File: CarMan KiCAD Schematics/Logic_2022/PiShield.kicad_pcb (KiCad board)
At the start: 2 copper layers, 57.8 x 76.4 mm, 20 parts, among them J1 J2 NI I2C, J2 J4 GLV BOB, J3 PICAN 2 Connector, J4 Motor Controller Header, J5 TSI Header, J6 PICAN 2 Connector, U1 RaspberryPi3, U10 BNO_055, U11 Raspberry_Pi_RTC

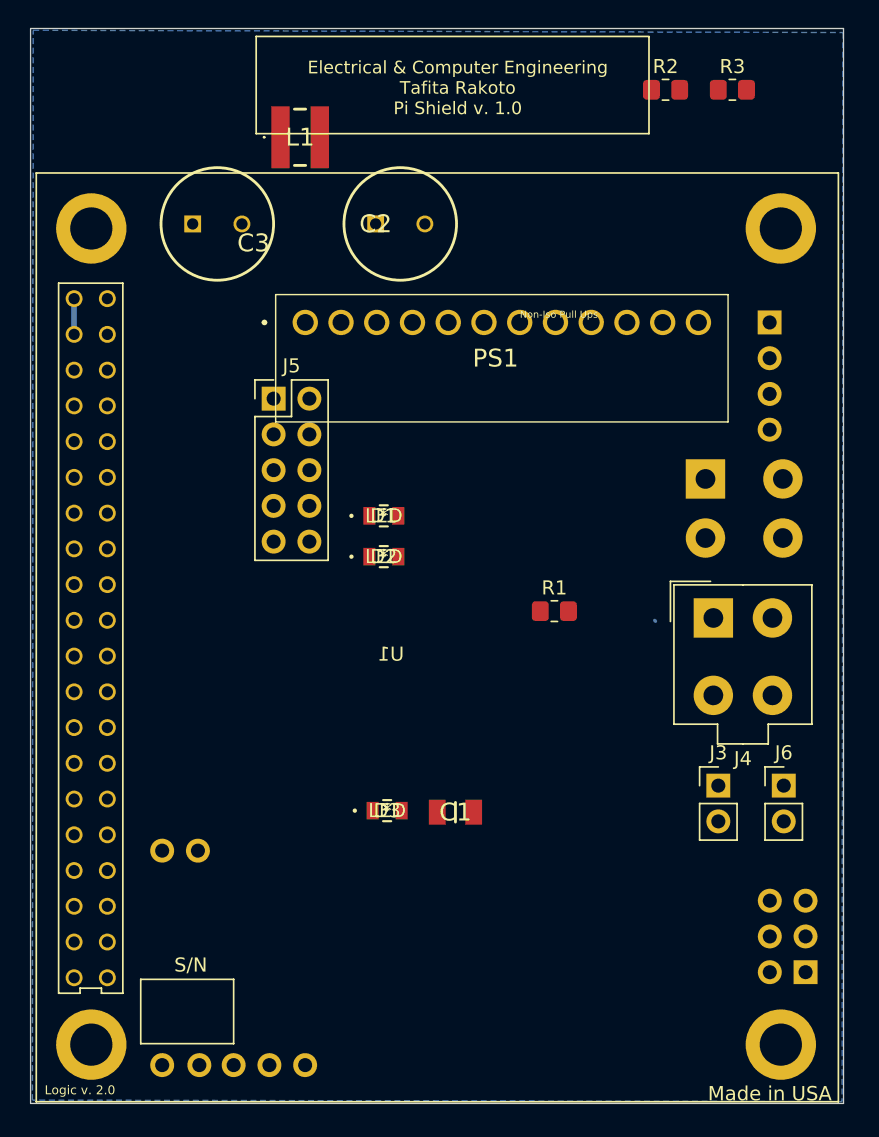
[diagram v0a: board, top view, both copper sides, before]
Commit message: Update the PCB layout with the wiring connected
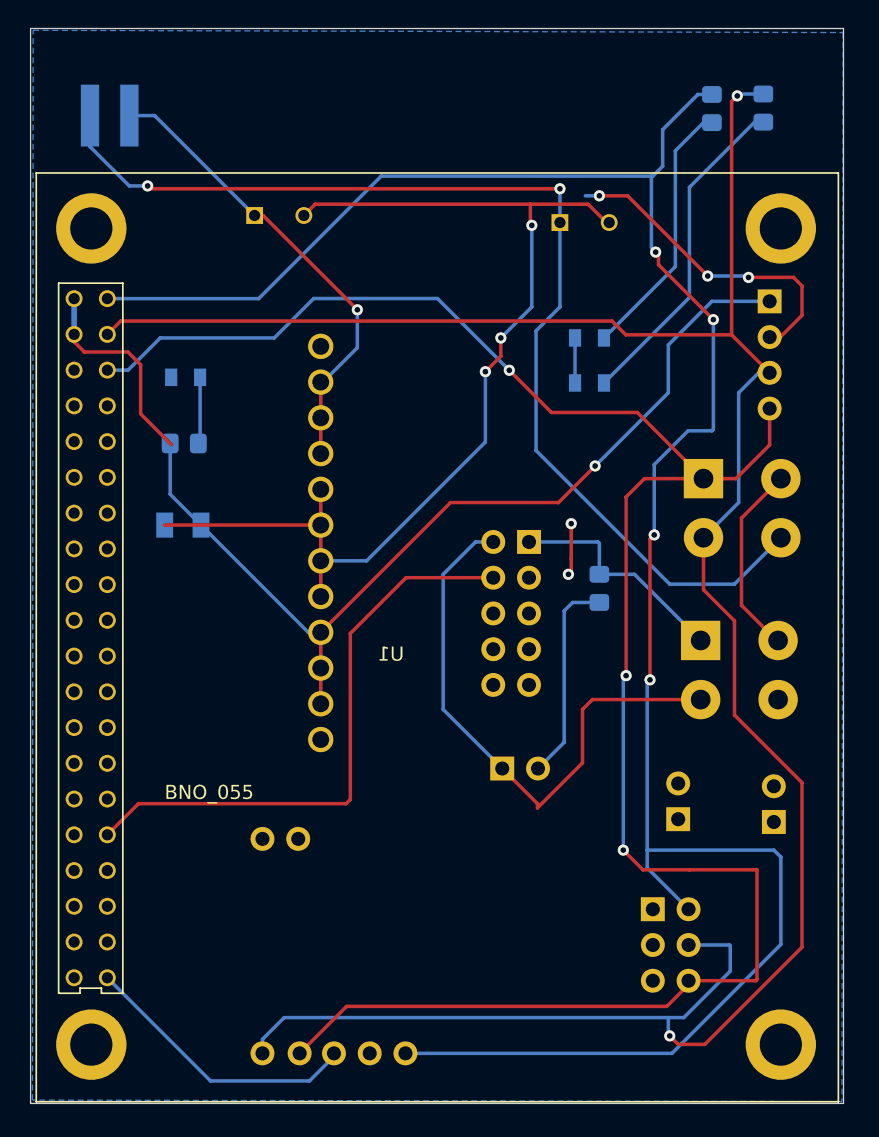
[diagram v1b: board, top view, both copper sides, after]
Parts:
- added J7: CAN Testing Header, Connector_PinHeader_2.54mm:PinHeader_1x02_P2.54mm_Vertical, B.Cu at (204.0, 91.7)
- added R4: 120, Resistor_SMD:R_0805_2012Metric_Pad1.20x1.40mm_HandSolder, B.Cu at (210.9, 78.9)
- C1, C2, C3, D1, D2, D3, J3, J4, J5, J6, L1, PS1, R1, R2, R3: moved to B.Cu
- moved D3 33.6 mm to (210.2, 64.3)
- moved R1 28.9 mm to (181.4, 68.6)
- moved C1 28.1 mm to (181.3, 74.4)
- moved D2 21.3 mm to (210.2, 61.1)
- moved J5 20.8 mm to (205.9, 75.6), turned to 180 degrees
- moved D1 17.2 mm to (181.5, 63.9)
- moved L1 13.6 mm to (176.1, 45.3)
- moved C2 13.1 mm to (208.1, 52.9)
- moved U11 11.7 mm to (214.7, 101.7), turned to 180 degrees
- moved U10 7.18 mm to (189.5, 96.7)
- moved C3 4.44 mm to (186.4, 52.4)
- moved J3 3.72 mm to (216.5, 95.3)
- moved R2 3.56 mm to (218.9, 44.8), turned to 270 degrees
- moved J6 2.68 mm to (223.3, 95.5)
- moved R3 2.56 mm to (222.6, 44.8), turned to 270 degrees
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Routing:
- net /SDA_PI: track 0.00 -> 169.0 mm, vias 0 -> 2
- net /3V3: track 0.00 -> 154.8 mm, vias 0 -> 4
- net /SCL_PI: track 0.00 -> 142.0 mm, vias 0 -> 3
- net /5V: track 2.61 -> 82.2 mm, vias 0 -> 1
- net /24V: track 0.00 -> 78.8 mm, vias 0 -> 2
- net Net-(C1-Pad1): track 0.00 -> 74.8 mm, vias 0 -> 3
- net /GLV_RTN: track 0.00 -> 63.8 mm, vias 0 -> 5
- net /SR_CTRL: track 0.00 -> 41.9 mm
- net /CAN_L: track 0.00 -> 40.9 mm
- net Net-(C3-Pad1): track 0.00 -> 33.3 mm, vias 0 -> 1
- net Net-(D3-Pad2): track 0.00 -> 23.6 mm
- net Net-(D2-Pad2): track 0.00 -> 18.8 mm
- net /CAN_H: track 0.57 -> 16.4 mm
- net Net-(J7-Pad2): track 0.00 -> 14.7 mm
- net Net-(D1-Pad2): track 0.00 -> 4.75 mm
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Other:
- board text removed: "Logic v. 2.0"
- board text removed: "Made in USA"
- board text removed: "Non-Iso Pull Ups"
- board text removed: "S/N"
- board text removed: "STATE LEDs"
- board text removed: "U10 IMU"
- board text removed: "U11 Pi RTC"

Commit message: Fixed the PCB layout wiring error detected by the rule checker
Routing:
- net (no net): track 0.56 -> 0.00 mm
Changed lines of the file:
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@@
     (thickness 1.6)
     (drawings 8)
-    (tracks 223)
+    (tracks 221)
     (zones 0)
     (modules 22)
@@
   (page A4)
   (layers
-    (0 F.Cu signal)
+    (0 F.Cu signal hide)
     (31 B.Cu signal)
-    (32 B.Adhes user hide)
-    (33 F.Adhes user hide)
-    (34 B.Paste user hide)
+    (32 B.Adhes user)
+    (33 F.Adhes user)
+    (34 B.Paste user)
     (35 F.Paste user)
     (36 B.SilkS user hide)
-    (37 F.SilkS user hide)
+    (37 F.SilkS user)
     (38 B.Mask user hide)
     (39 F.Mask user hide)
@@
     (effects (font (size 0.9 0.9) (thickness 0.15)) (justify mirror))
   )
-  (segment (start 176.0786 86.106) (end 175.9358 86.2488) (width 0.25) (layer B.Cu) (net 0) (status 30))
-  (segment (start 176.188346 86.501346) (end 175.9358 86.2488) (width 0.25) (layer B.Cu) (net 0) (status 30))
-  (segment (start 208.9 74.3) (end 208.9 76.8) (width 0.25) (layer F.Cu) (net 6))
-  (via (at 208.7 77.9) (size 0.8) (drill 0.4) (layers F.Cu B.Cu) (net 6))
-  (segment (start 208.9 77.7) (end 208.7 77.9) (width 0.25) (layer F.Cu) (net 6))
-  (segment (start 208.9 76.8) (end 208.9 77.7) (width 0.25) (layer F.Cu) (net 6))
-  (via (at 208.9 74.3) (size 0.8) (drill 0.4) (layers F.Cu B.Cu) (net 6))
   (segment (start 174.7 45.3) (end 174.7 47.5) (width 0.25) (layer B.Cu) (net 1) (status C00000))
   (segment (start 208.1 50.5) (end 208.1 52.9) (width 0.25) (layer B.Cu) (net 1) (status 800000))
@@
   (segment (start 193.2 82.1) (end 193.2 93.9) (width 0.25) (layer F.Cu) (net 5))
   (segment (start 197.16 78.14) (end 193.2 82.1) (width 0.25) (layer F.Cu) (net 5))
+  (segment (start 208.9 74.3) (end 208.9 76.8) (width 0.25) (layer F.Cu) (net 6))
+  (via (at 208.7 77.9) (size 0.8) (drill 0.4) (layers F.Cu B.Cu) (net 6))
+  (segment (start 208.9 77.7) (end 208.7 77.9) (width 0.25) (layer F.Cu) (net 6))
+  (segment (start 208.9 76.8) (end 208.9 77.7) (width 0.25) (layer F.Cu) (net 6))
+  (via (at 208.9 74.3) (size 0.8) (drill 0.4) (layers F.Cu B.Cu) (net 6))
   (segment (start 209.1713 61.1) (end 209.1713 64.3) (width 0.25) (layer B.Cu) (net 6) (status C00000))
   (segment (start 223.6 82.6) (end 223.5 82.6) (width 0.25) (layer F.Cu) (net 6) (status C00000))

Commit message: Updated the footprints
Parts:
- D1: value LED -> D1
- D2: value LED -> D2
- D3: value LED -> D3
- J1: value J2 NI I2C -> I2C Testing Header; footprint Connector_PinSocket_2.54mm:PinSocket_1x04_P2.54mm_Vertical -> Connector_PinHeader_2.54mm:PinHeader_1x04_P2.54mm_Vertical
- J2: value J4 GLV BOB -> J2
- J3: value PICAN 2 Connector -> J3
- J4: value Motor Controller Header -> J4
- J5: value TSI Header -> J5
- J6: value PICAN 2 Connector -> J6
- J7: value CAN Testing Header -> J7
- PS1: value Regulator -> PS1
